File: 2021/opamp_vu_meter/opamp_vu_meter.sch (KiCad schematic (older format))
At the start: 43 parts, among them J1 Conn_01x02, Q1 Q_PNP_BCE, U1 TLC272, U2 TLC272, U3 TLC272, U4 TLC272, U5 TLC272

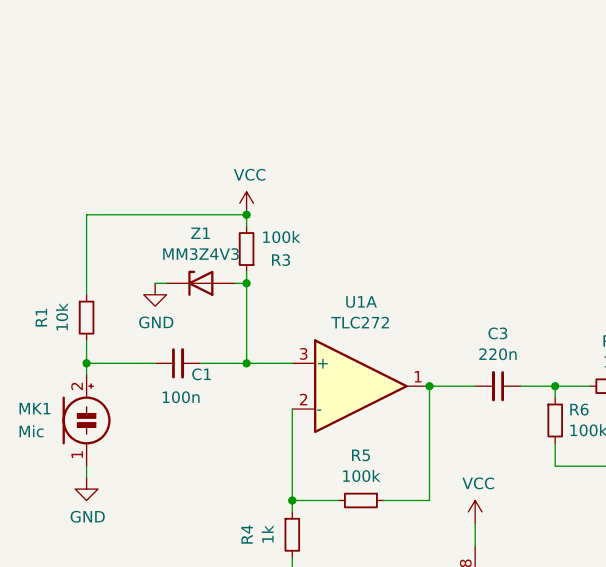
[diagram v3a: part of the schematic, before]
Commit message: Rotate one component
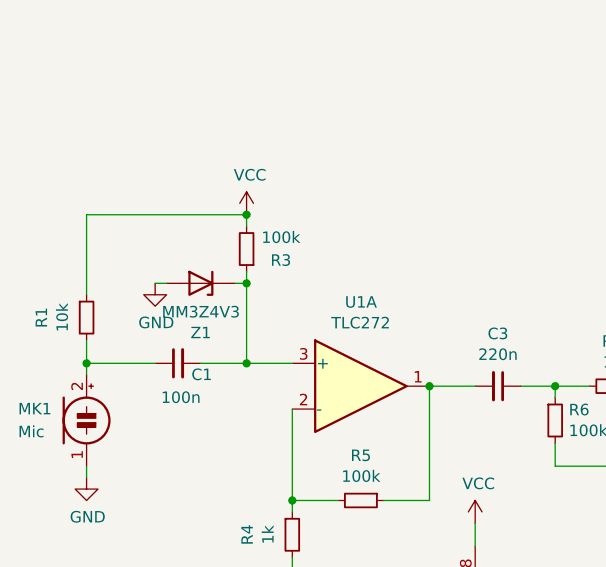
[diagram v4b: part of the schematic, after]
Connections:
- net GND: now also Z1.2 (A); no longer Z1.1 (K)
- net at C1.2, R3.1, U1.3 (+): now also Z1.1 (K); no longer Z1.2 (A)
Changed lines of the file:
@@
 F 3 "https://diotec.com/tl_files/diotec/files/pdf/datasheets/mm3z2v4.pdf" H 1350 5150 50  0001 C CNN
 	1    1350 5150
-	1    0    0    -1
+	-1   0    0    1
 $EndComp
 $EndSCHEMATC

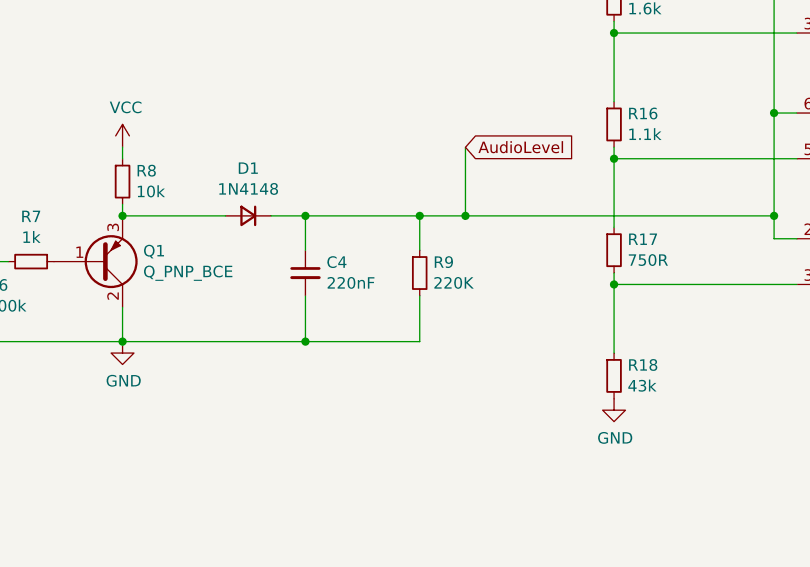
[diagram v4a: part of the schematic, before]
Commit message: Updated peak detector values
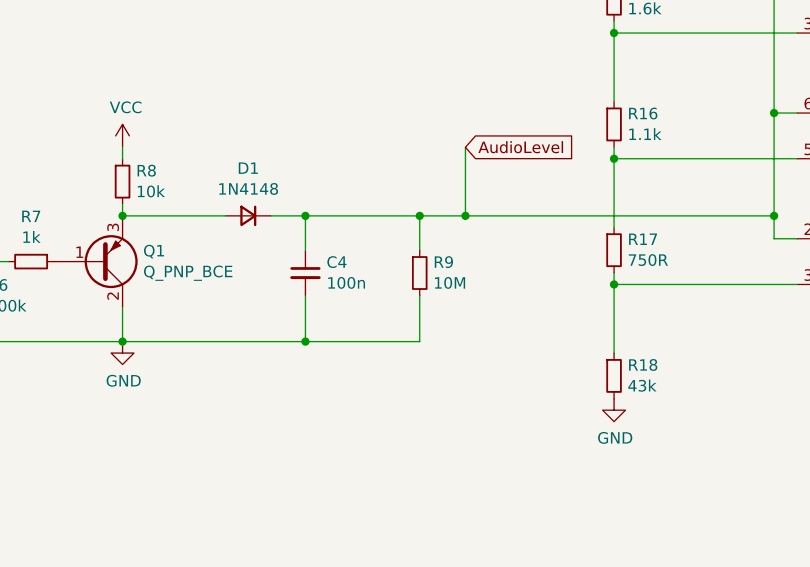
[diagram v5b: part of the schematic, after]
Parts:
- C4: value 220nF -> 100n
- R9: value 220K -> 10M
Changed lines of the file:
@@
 P 4850 5650
 F 0 "R9" H 4909 5696 50  0000 L CNN
-F 1 "220K" H 4909 5605 50  0000 L CNN
+F 1 "10M" H 4909 5605 50  0000 L CNN
 F 2 "Resistor_SMD:R_0805_2012Metric_Pad1.20x1.40mm_HandSolder" H 4850 5650 50  0001 C CNN
 F 3 "~" H 4850 5650 50  0001 C CNN
@@
 P 4350 5650
 F 0 "C4" H 4442 5696 50  0000 L CNN
-F 1 "220nF" H 4442 5605 50  0000 L CNN
+F 1 "100n" H 4442 5605 50  0000 L CNN
 F 2 "Capacitor_SMD:C_0805_2012Metric_Pad1.18x1.45mm_HandSolder" H 4350 5650 50  0001 C CNN
 F 3 "~" H 4350 5650 50  0001 C CNN
